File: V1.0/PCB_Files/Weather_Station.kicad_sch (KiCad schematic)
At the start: 38 parts, among them J1 N091-2832TSWFG02-H14, J2 USB_B_Micro, J3 Conn_01x04_Pin, U1 STM32F103C8T6, U2 HDC1080DMBR, U3 AMS1117-3.3, U5 SRV05-4, Y1 X322516MLB4SI

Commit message: Schematic should be 90% finished. Finishing touches and then design review.
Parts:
- added J4: Conn_01x04_Pin, Connector_PinHeader_1.00mm:PinHeader_1x04_P1.00mm_Vertical, symbol Connector:Conn_01x04_Pin
- C22: value 10uF/10V -> 22u/10V; footprint (none) -> Capacitor_SMD:C_0805_2012Metric
- C23: value C -> 22u/10V; footprint (none) -> Capacitor_SMD:C_0805_2012Metric
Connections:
- net +3.3V: no longer C1.1, C13.1, C14.1, C19.1, C2.1, C20.1, C21.2, C3.1, C4.1, C5.1, C6.1, FB1.2, J1.5 (Pin_5), J1.8 (Pin_8), J1.9 (Pin_9), R3.1, U1.24 (VDD), U1.36 (VDD), U1.48 (VDD)
- net +3.3VA: no longer C7.1, C8.1, FB1.1
- net GND: no longer C1.2, C12.1, C13.2, C14.2, C15.2, C19.2, C2.2, C20.2, C21.1, C22.2, C23.2, C3.2, C4.2, C5.2, C8.2, R4.2, U1.8 (VSSA), Y1.2, Y1.4
- net OSC_IN: no longer Y1.3
- net OSC_OUT: no longer Y1.1
- net SWCLK: now also J4.3 (Pin_3)
- net SWDIO: now also J4.4 (Pin_4)
- net USART1_RX: now also J4.2 (Pin_2)
- net USART1_TX: now also J4.1 (Pin_1)
- new net: C22.2, C23.2
- no-connect marks 3 -> 29
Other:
- note added: "Inputs"
- note added: "UART + Serial Wire"
- moved on the sheet: C22, C23, F1, J2, R5, U3, U5

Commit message: Weird schematic error fixed.
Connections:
- net +3.3V: now also C1.1, C13.1, C14.1, C19.1, C2.1, C20.1, C21.2, C3.1, C4.1, C5.1, C6.1, FB1.2, J1.5 (Pin_5), J1.8 (Pin_8), J1.9 (Pin_9), R3.1, U1.24 (VDD), U1.36 (VDD), U1.48 (VDD)
- net +3.3VA: now also C7.1, C8.1, FB1.1
- net GND: now also C1.2, C12.1, C13.2, C14.2, C15.2, C19.2, C2.2, C20.2, C21.1, C3.2, C4.2, C5.2, C8.2, R4.2, U1.8 (VSSA), Y1.2, Y1.4
- net OSC_IN: now also Y1.3
- net OSC_OUT: now also Y1.1
- no-connect marks 29 -> 31

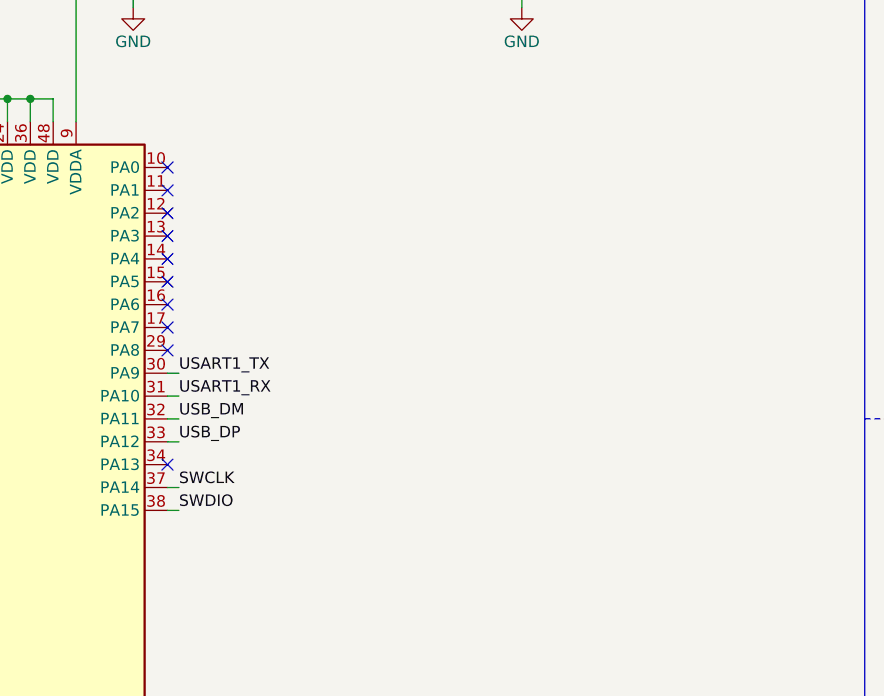
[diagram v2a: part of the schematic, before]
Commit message: Added Debug Leds.
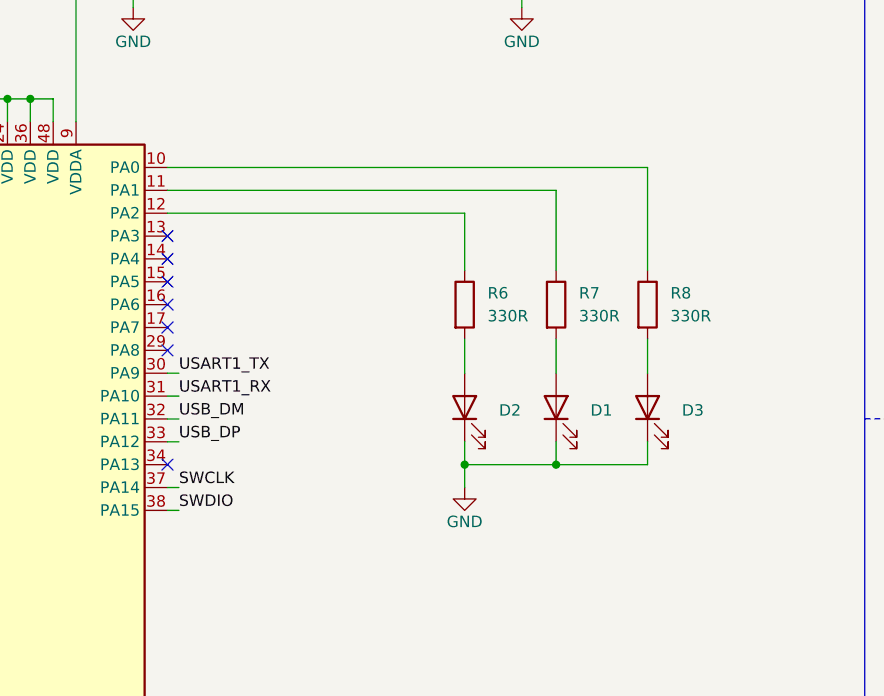
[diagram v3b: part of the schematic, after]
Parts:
- added D1: KT-0603W, LED_SMD:LED_0603_1608Metric, symbol Device:LED
- added D2: KT-0603R, LED_SMD:LED_0603_1608Metric, symbol Device:LED
- added D3: 19-217/BHC-ZL1M2RY/6T, LED_SMD:LED_0603_1608Metric, symbol Device:LED
- added R6, R7, R8: 330R, Resistor_SMD:R_0603_1608Metric, symbol Device:R
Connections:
- net GND: now also D1.1 (K), D2.1 (K), D3.1 (K)
- net at U1.10 (PA0): now also R8.1
- net at U1.11 (PA1): now also R7.1
- net at U1.12 (PA2): now also R6.1
- new net: D3.2 (A), R8.2
- new net: D1.2 (A), R7.2
- new net: D2.2 (A), R6.2
- no-connect marks 31 -> 28

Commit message: Started Layout of PCB.
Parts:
- removed C5: 100n/10V, Capacitor_SMD:C_0603_1608Metric, symbol Device:C
- Y1: footprint (none) -> Crystal:Crystal_SMD_3225-4Pin_3.2x2.5mm
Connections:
- net LED_B: now reaches R8.1, U1.10 (PA0)
- net LED_R: now reaches R6.1, U1.12 (PA2)
- net LED_W: now reaches R7.1, U1.11 (PA1)
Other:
- moved on the sheet: C6
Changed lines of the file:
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@@
 	)
 	(junction
-		(at 40.64 36.83)
-		(diameter 0)
-		(color 0 0 0 0)
-	)
-	(junction
 		(at 76.2 36.83)
 		(diameter 0)
@@
 	)
 	(junction
-		(at 24.13 46.99)
-		(diameter 0)
-		(color 0 0 0 0)
-	)
-	(junction
 		(at 137.16 198.12)
 		(diameter 0)
@@
 	(wire
 		(pts
-			(xy 24.13 46.99) (xy 24.13 48.26)
+			(xy 40.64 46.99) (xy 40.64 49.53)
 		)
 		(stroke
@@
 	(wire
 		(pts
-			(xy 24.13 45.72) (xy 24.13 46.99)
-		)
-		(stroke
-			(width 0)
-			(type default)
-		)
-	)
-	(wire
-		(pts
 			(xy 147.32 96.52) (xy 148.59 96.52)
 		)
@@
 	(wire
 		(pts
-			(xy 24.13 38.1) (xy 24.13 36.83)
-		)
-		(stroke
-			(width 0)
-			(type default)
-		)
-	)
-	(wire
-		(pts
 			(xy 180.34 99.06) (xy 180.34 101.6)
 		)
@@
 	(wire
 		(pts
-			(xy 24.13 36.83) (xy 40.64 36.83)
-		)
-		(stroke
-			(width 0)
-			(type default)
-		)
-	)
-	(wire
-		(pts
 			(xy 93.98 36.83) (xy 93.98 38.1)
 		)
@@
 	(wire
 		(pts
-			(xy 24.13 46.99) (xy 40.64 46.99)
-		)
-		(stroke
-			(width 0)
-			(type default)
-		)
-	)
-	(wire
-		(pts
 			(xy 41.91 90.17) (xy 41.91 97.79)
 		)
@@
 		)
 	)
+	(label "LED_W"
+		(at 148.59 68.58 0)
+		(fields_autoplaced yes)
+		(effects
+			(font
+				(size 1.27 1.27)
+			)
+			(justify left bottom)
+		)
+	)
 	(label "SWDIO"
 		(at 148.59 104.14 0)
@@
 		)
 	)
+	(label "LED_R"
+		(at 148.59 71.12 0)
+		(fields_autoplaced yes)
+		(effects
+			(font
+				(size 1.27 1.27)
+			)
+			(justify left bottom)
+		)
+	)
+	(label "LED_B"
+		(at 148.59 66.04 0)
+		(fields_autoplaced yes)
+		(effects
+			(font
+				(size 1.27 1.27)
+			)
+			(justify left bottom)
+		)
+	)
 	(label "BOOT0"
 		(at 105.41 71.12 0)
@@
 	)
 	(symbol
-		(lib_id "Device:C")
-		(at 40.64 41.91 0)
-		(unit 1)
-		(exclude_from_sim no)
-		(in_bom yes)
-		(on_board yes)
-		(dnp no)
-		(fields_autoplaced yes)
-		(property "Reference" "C5"
-			(at 44.45 40.6399 0)
-			(effects
-				(font
-					(size 1.27 1.27)
-				)
-				(justify left)
-			)
-		)
-		(property "Value" "100n/10V"
-			(at 44.45 43.1799 0)
-			(effects
-				(font
-					(size 1.27 1.27)
-				)
-				(justify left)
-			)
-		)
-		(property "Footprint" "Capacitor_SMD:C_0603_1608Metric"
-			(at 41.6052 45.72 0)
-			(effects
-				(font
-					(size 1.27 1.27)
-				)
-				(hide yes)
-			)
-		)
-		(property "Datasheet" "~"
-			(at 40.64 41.91 0)
-			(effects
-				(font
-					(size 1.27 1.27)
-				)
-				(hide yes)
-			)
-		)
-		(property "Description" "Unpolarized capacitor"
-			(at 40.64 41.91 0)
-			(effects
-				(font
-					(size 1.27 1.27)
-				)
-				(hide yes)
-			)
-		)
-		(pin "2"
-		)
-		(pin "1"
-		)
-		(instances
-			(project "Weather_Station"
-				(path "/480d2398-431a-4c09-b50a-21d5fdc9f45a"
-					(reference "C5")
-					(unit 1)
-				)
-			)
-		)
-	)
-	(symbol
 		(lib_id "Device:R")
 		(at 88.9 102.87 0)
@@
 	(symbol
 		(lib_id "power:GND")
-		(at 24.13 48.26 0)
+		(at 40.64 49.53 0)
 		(unit 1)
 		(exclude_from_sim no)
@@
 		(dnp no)
 		(property "Reference" "#PWR03"
-			(at 24.13 54.61 0)
+			(at 40.64 55.88 0)
 			(effects
 				(font
@@
 		)
 		(property "Value" "GND"
-			(at 24.13 52.07 0)
+			(at 40.64 53.34 0)
 			(effects
 				(font
@@
 		)
 		(property "Footprint" ""
-			(at 24.13 48.26 0)
+			(at 40.64 49.53 0)
 			(effects
 				(font
@@
 		)
 		(property "Datasheet" ""
-			(at 24.13 48.26 0)
+			(at 40.64 49.53 0)
 			(effects
 				(font
@@
 		)
 		(property "Description" "Power symbol creates a global label with name \"GND\" , ground"
-			(at 24.13 48.26 0)
+			(at 40.64 49.53 0)
 			(effects
 				(font
@@
 			)
 		)
-		(property "Footprint" ""
+		(property "Footprint" "Crystal:Crystal_SMD_3225-4Pin_3.2x2.5mm"
 			(at 59.69 97.79 0)
 			(effects
@@
 	(symbol
 		(lib_id "Device:C")
-		(at 24.13 41.91 0)
+		(at 40.64 41.91 0)
 		(unit 1)
 		(exclude_from_sim no)
@@
 		(fields_autoplaced yes)
 		(property "Reference" "C6"
-			(at 27.94 40.6399 0)
+			(at 44.45 40.6399 0)
 			(effects
 				(font
@@
 		)
 		(property "Value" "10u/10V"
-			(at 27.94 43.1799 0)
+			(at 44.45 43.1799 0)
 			(effects
 				(font
@@
 		)
 		(property "Footprint" "Capacitor_SMD:C_0805_2012Metric"
-			(at 25.0952 45.72 0)
+			(at 41.6052 45.72 0)
 			(effects
 				(font
@@
 		)
 		(property "Datasheet" "~"
-			(at 24.13 41.91 0)
+			(at 40.64 41.91 0)
 			(effects
 				(font
@@
 		)
 		(property "Description" "Unpolarized capacitor"
-			(at 24.13 41.91 0)
+			(at 40.64 41.91 0)
 			(effects
 				(font

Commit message: Made Progress with STM32 Layout.
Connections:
- net GND: now also C22.2, C23.2
- net VBUS: now also R5.1, U5.5 (VP)
- net VBUS_IN: now reaches F1.2, J2.1 (VBUS)
- net VBUS_IN: no longer R5.1, U5.5 (VP)
- net USB_DM renamed USB_D-
- net USB_DP renamed USB_D+
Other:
- moved on the sheet: F1
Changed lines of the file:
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@@
 	)
 	(junction
-		(at 295.91 40.64)
+		(at 156.21 213.36)
 		(diameter 0)
 		(color 0 0 0 0)
 	)
 	(junction
-		(at 156.21 213.36)
+		(at 289.56 186.69)
 		(diameter 0)
 		(color 0 0 0 0)
@@
 	)
 	(junction
-		(at 111.76 36.83)
+		(at 316.23 29.21)
 		(diameter 0)
 		(color 0 0 0 0)
 	)
 	(junction
-		(at 76.2 46.99)
+		(at 111.76 36.83)
 		(diameter 0)
 		(color 0 0 0 0)
 	)
 	(junction
-		(at 129.54 58.42)
+		(at 76.2 46.99)
 		(diameter 0)
 		(color 0 0 0 0)
 	)
 	(junction
-		(at 323.85 40.64)
+		(at 129.54 58.42)
 		(diameter 0)
 		(color 0 0 0 0)
@@
 	)
 	(junction
+		(at 295.91 29.21)
+		(diameter 0)
+		(color 0 0 0 0)
+	)
+	(junction
 		(at 156.21 223.52)
 		(diameter 0)
@@
 	(wire
 		(pts
-			(xy 323.85 40.64) (xy 323.85 48.26)
+			(xy 316.23 41.91) (xy 316.23 48.26)
 		)
 		(stroke
@@
 	(wire
 		(pts
-			(xy 289.56 184.15) (xy 289.56 187.96)
-		)
-		(stroke
-			(width 0)
-			(type default)
-		)
-	)
-	(wire
-		(pts
 			(xy 156.21 223.52) (xy 156.21 222.25)
 		)
@@
 	(wire
 		(pts
-			(xy 295.91 40.64) (xy 323.85 40.64)
-		)
-		(stroke
-			(width 0)
-			(type default)
-		)
-	)
-	(wire
-		(pts
 			(xy 127 30.48) (xy 127 36.83)
 		)
@@
 	(wire
 		(pts
-			(xy 280.67 40.64) (xy 295.91 40.64)
+			(xy 280.67 29.21) (xy 295.91 29.21)
 		)
 		(stroke
@@
 	(wire
 		(pts
+			(xy 309.88 186.69) (xy 289.56 186.69)
+		)
+		(stroke
+			(width 0)
+			(type default)
+		)
+	)
+	(wire
+		(pts
 			(xy 73.66 71.12) (xy 73.66 72.39)
 		)
@@
 	(wire
 		(pts
-			(xy 323.85 48.26) (xy 325.12 48.26)
+			(xy 316.23 48.26) (xy 325.12 48.26)
 		)
 		(stroke
@@
 	(wire
 		(pts
-			(xy 295.91 40.64) (xy 295.91 41.91)
-		)
-		(stroke
-			(width 0)
-			(type default)
-		)
-	)
-	(wire
-		(pts
 			(xy 73.66 71.12) (xy 73.66 69.85)
 		)
@@
 	(wire
 		(pts
-			(xy 264.16 186.69) (xy 309.88 186.69)
+			(xy 190.5 99.06) (xy 190.5 96.52)
 		)
 		(stroke
@@
 	(wire
 		(pts
-			(xy 190.5 99.06) (xy 190.5 96.52)
+			(xy 316.23 29.21) (xy 316.23 34.29)
 		)
 		(stroke
@@
 	(wire
 		(pts
+			(xy 289.56 184.15) (xy 289.56 186.69)
+		)
+		(stroke
+			(width 0)
+			(type default)
+		)
+	)
+	(wire
+		(pts
 			(xy 147.32 88.9) (xy 148.59 88.9)
 		)
@@
 	(wire
 		(pts
+			(xy 264.16 186.69) (xy 289.56 186.69)
+		)
+		(stroke
+			(width 0)
+			(type default)
+		)
+	)
+	(wire
+		(pts
 			(xy 134.62 185.42) (xy 158.75 185.42)
 		)
@@
 	(wire
 		(pts
-			(xy 280.67 72.39) (xy 280.67 40.64)
+			(xy 280.67 72.39) (xy 280.67 29.21)
 		)
 		(stroke
@@
 	(wire
 		(pts
-			(xy 323.85 27.94) (xy 323.85 30.48)
+			(xy 316.23 25.4) (xy 316.23 29.21)
 		)
 		(stroke
@@
 	(wire
 		(pts
+			(xy 295.91 29.21) (xy 295.91 41.91)
+		)
+		(stroke
+			(width 0)
+			(type default)
+		)
+	)
+	(wire
+		(pts
 			(xy 41.91 90.17) (xy 41.91 97.79)
 		)
@@
 	(wire
 		(pts
-			(xy 323.85 38.1) (xy 323.85 40.64)
-		)
-		(stroke
-			(width 0)
-			(type default)
-		)
-	)
-	(wire
-		(pts
 			(xy 134.62 187.96) (xy 163.83 187.96)
 		)
@@
 	(wire
 		(pts
+			(xy 289.56 186.69) (xy 289.56 187.96)
+		)
+		(stroke
+			(width 0)
+			(type default)
+		)
+	)
+	(wire
+		(pts
 			(xy 163.83 181.61) (xy 163.83 187.96)
 		)
@@
 	(wire
 		(pts
+			(xy 295.91 29.21) (xy 316.23 29.21)
+		)
+		(stroke
+			(width 0)
+			(type default)
+		)
+	)
+	(wire
+		(pts
 			(xy 200.66 199.39) (xy 200.66 200.66)
 		)
@@
 		)
 	)
-	(label "USB_DM"
+	(label "USB_D-"
 		(at 148.59 93.98 0)
 		(fields_autoplaced yes)
@@
 		)
 	)
-	(label "USB_DP"
+	(label "USB_D+"
 		(at 148.59 96.52 0)
 		(fields_autoplaced yes)
@@
 		)
 	)
-	(label "USB_DM"
+	(label "USB_D-"
 		(at 313.69 55.88 0)
 		(fields_autoplaced yes)
@@
 		)
 	)
-	(label "USB_DP"
+	(label "USB_D+"
 		(at 313.69 53.34 0)
 		(fields_autoplaced yes)
@@
 		)
 	)
+	(label "VBUS_IN"
+		(at 325.12 48.26 180)
+		(fields_autoplaced yes)
+		(effects
+			(font
+				(size 1.27 1.27)
+			)
+			(justify right bottom)
+		)
+	)
 	(label "I2C1_SCL"
 		(at 83.82 207.01 180)
@@
 	(symbol
 		(lib_id "power:VBUS")
-		(at 323.85 27.94 0)
+		(at 316.23 25.4 0)
 		(unit 1)
 		(exclude_from_sim no)
@@
 		(dnp no)
 		(property "Reference" "#PWR022"
-			(at 323.85 31.75 0)
+			(at 316.23 29.21 0)
 			(effects
 				(font
@@
 		)
 		(property "Value" "VBUS"
-			(at 323.85 24.13 0)
+			(at 316.23 21.59 0)
 			(effects
 				(font
@@
 		)
 		(property "Footprint" ""
-			(at 323.85 27.94 0)
+			(at 316.23 25.4 0)
 			(effects
 				(font
@@
 		)
 		(property "Datasheet" ""
-			(at 323.85 27.94 0)
+			(at 316.23 25.4 0)
 			(effects
 				(font
@@
 		)
 		(property "Description" "Power symbol creates a global label with name \"VBUS\""
-			(at 323.85 27.94 0)
+			(at 316.23 25.4 0)
 			(effects
 				(font
@@
 	(symbol
 		(lib_id "Device:Fuse")
-		(at 323.85 34.29 0)
+		(at 316.23 38.1 0)
 		(unit 1)
 		(exclude_from_sim no)
@@
 		(fields_autoplaced yes)
 		(property "Reference" "F1"
-			(at 326.39 33.0199 0)
+			(at 318.77 36.8299 0)
 			(effects
 				(font
@@
 		)
 		(property "Value" "JFC1206-1100FS"
-			(at 326.39 35.5599 0)
+			(at 318.77 39.3699 0)
 			(effects
 				(font
@@
 		)
 		(property "Footprint" "Fuse:Fuse_1206_3216Metric"
-			(at 322.072 34.29 90)
+			(at 314.452 38.1 90)
 			(effects
 				(font
@@
 		)
 		(property "Datasheet" "~"
-			(at 323.85 34.29 0)
+			(at 316.23 38.1 0)
 			(effects
 				(font
@@
 		)
 		(property "Description" "63V / 1A"
-			(at 323.85 34.29 0)
+			(at 316.23 38.1 0)
 			(effects
 				(font

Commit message: Changed USART1 to USART3. Finished LDO Layout. Finished ESD protection of micro USB.
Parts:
- added J5: Conn_01x06_Pin, Connector_PinHeader_1.00mm:PinHeader_1x06_P1.00mm_Vertical, symbol Connector:Conn_01x06_Pin
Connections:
- net GND: now also J5.2 (Pin_2)
- net I2C1_SCL: now also J5.4 (Pin_4)
- net I2C1_SDA: now also J5.3 (Pin_3)
- net USB_D+: now also U5.6 (IO4)
- net USB_D-: now also U5.4 (IO3)
- net VBUS: now also J5.1 (Pin_1)
- net USART3_TX: now reaches U1.21 (PB10)
- net USART3_TX: now also J4.1 (Pin_1)
- net USART3_RX: now reaches U1.22 (PB11)
- net USART3_RX: now also J4.2 (Pin_2)
- net USART1_RX: no longer names the net of U1.31 (PA10)
- net USART1_RX: no longer J4.2 (Pin_2)
- net USART1_TX: no longer names the net of U1.30 (PA9)
- net USART1_TX: no longer J4.1 (Pin_1)
- new net RTC_CLK: J5.5 (Pin_5)
- new net RTC_INT: J5.6 (Pin_6)
- no-connect marks 28 -> 24
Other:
- note added: "Check Pullup and Pulldown."
- note added: "RTC-Module"
- note added: "ToDo: Check Display Power on each Line."

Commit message: Changed back to USART_1.
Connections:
- net USART1_TX: now reaches U1.30 (PA9)
- net USART1_TX: now also J4.1 (Pin_1)
- net USART1_RX: now reaches U1.31 (PA10)
- net USART1_RX: now also J4.2 (Pin_2)
- net USART3_RX: no longer names the net of U1.22 (PB11)
- net USART3_RX: no longer J4.2 (Pin_2)
- net USART3_TX: no longer names the net of U1.21 (PB10)
- net USART3_TX: no longer J4.1 (Pin_1)
- no-connect marks 24 -> 26
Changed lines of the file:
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@@
+	)
+	(no_connect
+		(at 114.3 119.38)
 	)
 	(no_connect
@@
 	)
 	(no_connect
+		(at 114.3 121.92)
+	)
+	(no_connect
 		(at 147.32 99.06)
 	)
@@
 	(wire
 		(pts
-			(xy 113.03 121.92) (xy 114.3 121.92)
-		)
-		(stroke
-			(width 0)
-			(type default)
-		)
-	)
-	(wire
-		(pts
 			(xy 76.2 36.83) (xy 93.98 36.83)
 		)
@@
 		(pts
 			(xy 156.21 213.36) (xy 156.21 214.63)
-		)
-		(stroke
-			(width 0)
-			(type default)
-		)
-	)
-	(wire
-		(pts
-			(xy 113.03 119.38) (xy 114.3 119.38)
 		)
 		(stroke
@@
 		)
 	)
-	(label "USART3_RX"
+	(label "USART1_RX"
 		(at 260.35 115.57 0)
 		(fields_autoplaced yes)
@@
 		)
 	)
-	(label "USART3_TX"
+	(label "USART1_TX"
 		(at 260.35 113.03 0)
 		(fields_autoplaced yes)
@@
 		)
 	)
-	(label "USART3_RX"
-		(at 113.03 121.92 180)
-		(fields_autoplaced yes)
-		(effects
-			(font
-				(size 1.27 1.27)
-			)
-			(justify right bottom)
+	(label "USART1_RX"
+		(at 148.59 91.44 0)
+		(fields_autoplaced yes)
+		(effects
+			(font
+				(size 1.27 1.27)
+			)
+			(justify left bottom)
 		)
 	)
@@
 		)
 	)
-	(label "USART3_TX"
-		(at 113.03 119.38 180)
-		(fields_autoplaced yes)
-		(effects
-			(font
-				(size 1.27 1.27)
-			)
-			(justify right bottom)
-		)
-	)
+	(label "USART1_TX"
+		(at 148.59 88.9 0)
+		(fields_autoplaced yes)
+		(effects
+			(font
+				(size 1.27 1.27)
+			)
+			(justify left bottom)
+		)
+	)
